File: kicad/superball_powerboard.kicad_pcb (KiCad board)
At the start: 4 copper layers, 100 x 50 mm, 149 parts, among them J1 MICROCLASP_HDRX3, J2 MICROCLASP_HDRX3, J3 MICROCLASP_HDRX2, J4 MICROCLASP_HDRX2, J5 MICROCLASP_HDRX2, J6 MICROCLASP_HDRX2, J7 MICROCLASP_HDRX2, J8 MICROCLASP_HDRX2, J9 MICROCLASP_HDRX2, Q1 MCP73832, Q10 FDS6898AZ, Q11 FDS6898AZ, Q12 LTC1982, Q13 LTC1982, Q14 FDS6898AZ, Q15 FDS6898AZ, Q16 RF803D, Q2 LM3478, Q3 TPS54540, Q4 LT1910, Q5 0S102011MA1QN1, Q6 PSMN013-80YS, Q7 PSMN013-80YS, Q8 LTC1982, Q9 ACS711KLCTR-12AB-T, U1 SI1970DH, U2 CSD16323Q3, U3 SN65HVD232, U4 DSPIC33E128MC506, U5 LDO 3V3 SOT-223

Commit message: started organizing the pcb layout
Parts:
- added ?: P***, 1pin_3mm, F.Cu at (116.6, 24.5)
- added ?: P***, 1pin_3mm, F.Cu at (116.6, 64.8)
- added ?: P***, 1pin_3mm, F.Cu at (23.5, 24.5)
- added ?: P***, 1pin_3mm, F.Cu at (23.5, 64.8)
- added R55: 10K, SM0805, F.Cu at (75.0, 85.0)
- added R56: 10K, SM0805, F.Cu at (70.0, 82.8)
- moved JP11 196.4 mm to (26.0, 54.0)
- moved JP12 133.1 mm to (27.0, 41.0), turned to 90 degrees
- moved JP8 127.0 mm to (85.5, 53.0), turned to 90 degrees
- moved JP6 99.7 mm to (116.5, 40.5), turned to 90 degrees
- moved JP7 96.3 mm to (85.5, 59.0), turned to 90 degrees
- moved C1 74.7 mm to (114.0, 53.5), turned to 90 degrees
- moved JP5 69.1 mm to (61.0, 67.5)
- moved JP4 35.7 mm to (28.5, 31.5), turned to 180 degrees
- moved J9 34.7 mm to (57.0, 68.0), turned to 180 degrees
- moved Q9 23.6 mm to (113.5, 47.5)
- moved J8 20.5 mm to (48.5, 68.0)
- moved JP1 18.5 mm to (34.0, 67.5)
- moved U3 16.6 mm to (48.0, 33.5)
- moved Q5 14.5 mm to (80.5, 68.0)
- moved JP10 7.24 mm to (22.5, 47.5)
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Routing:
- net N-0000041: track 0.00 -> 22.2 mm
- net /CAN_L: track 21.3 -> 1.04 mm
- net /CAN_H: track 15.3 -> 33.6 mm
- net GND: track 0.00 -> 16.2 mm
- net (no net): track 0.00 -> 8.09 mm

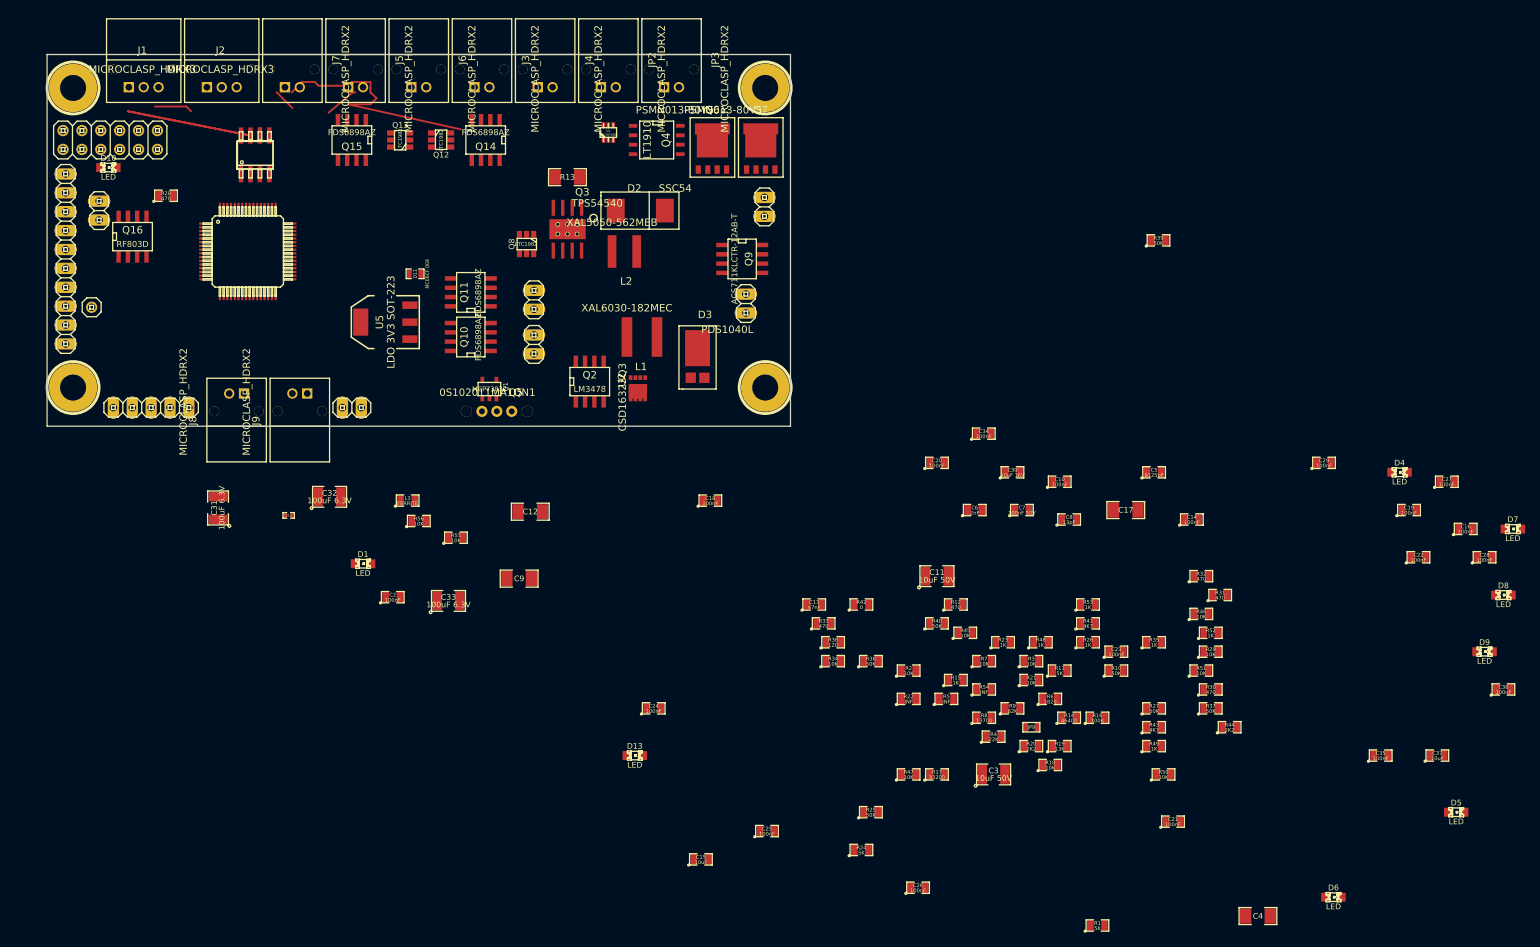
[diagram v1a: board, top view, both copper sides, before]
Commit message: did initial placement of the components on the pcb
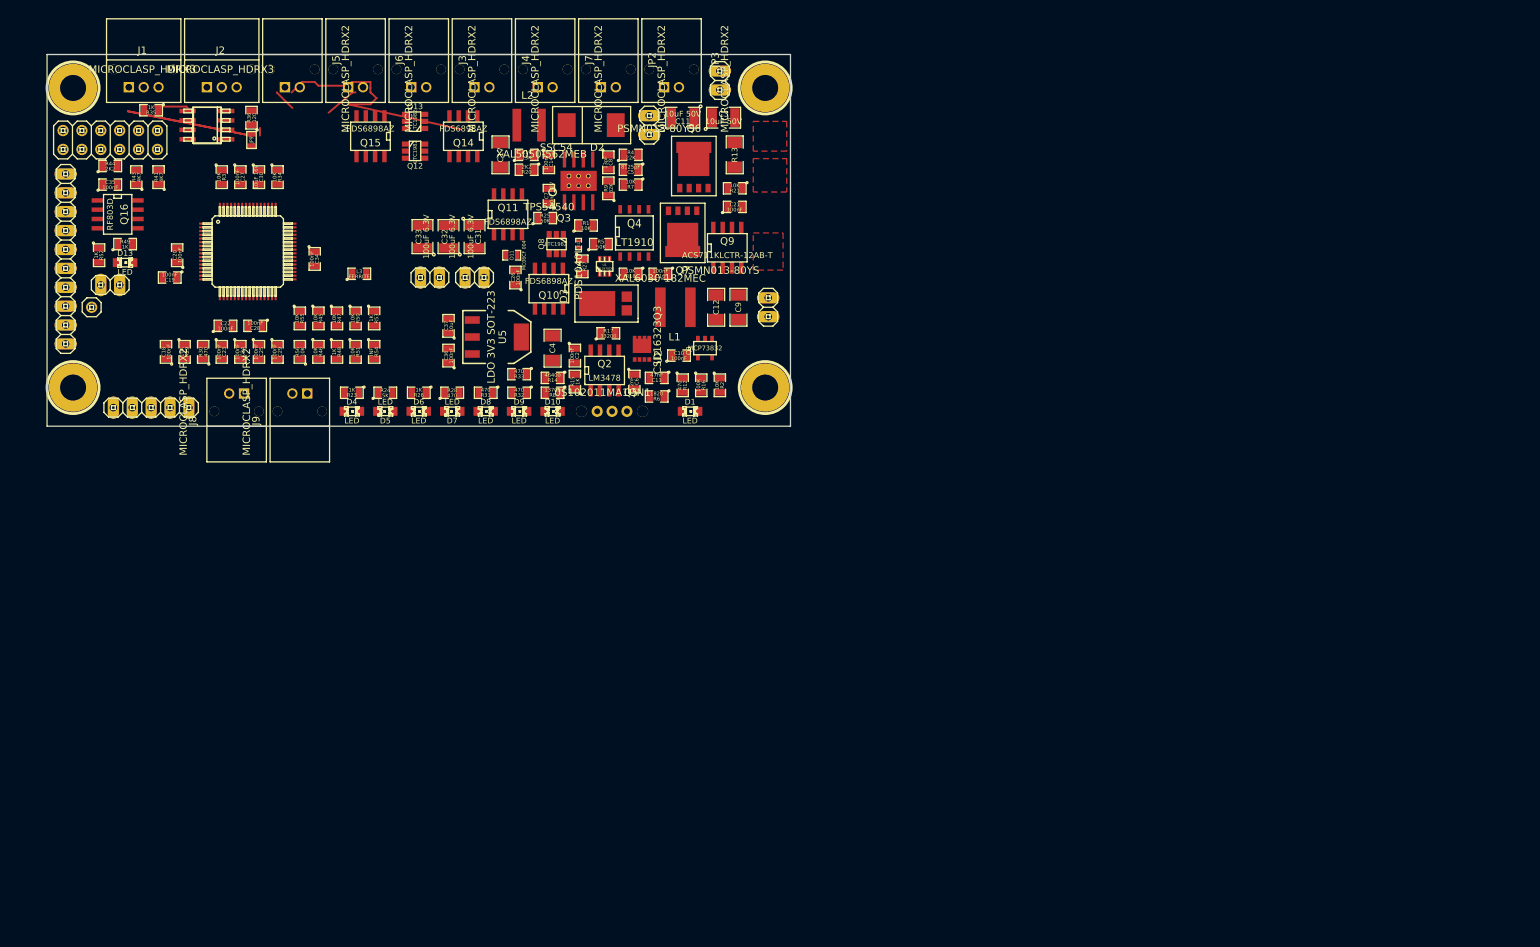
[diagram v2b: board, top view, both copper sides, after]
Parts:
- removed C15: 10uF, SM0805
- removed R10, R37, R38, R39, R40: 50K, SM0805
- removed R11: 5K, SM0805
- removed R22: INF, SM0805
- removed R42: 0, SM0805
- R1: value 5K -> 10K
- R5: value INF -> 50K
- moved C35 187.4 mm to (28.5, 37.5)
- moved C19 169.6 mm to (36.5, 50.0), turned to 180 degrees
- moved R44 168.4 mm to (28.5, 35.0)
- moved C28 168.3 mm to (48.0, 56.5), turned to 180 degrees
- moved C27 167.4 mm to (46.0, 36.5), turned to 270 degrees
- moved C22 163.5 mm to (44.0, 56.5)
- moved R52 157.9 mm to (27.0, 47.0), turned to 270 degrees
- moved R43 155.6 mm to (32.0, 36.5), turned to 90 degrees
- moved R49 154.0 mm to (30.5, 45.5)
- moved D5 153.8 mm to (65.5, 68.0), turned to 180 degrees
- moved R35 152.7 mm to (34.0, 27.5), turned to 180 degrees
- moved C36 148.8 mm to (74.0, 60.5), turned to 90 degrees
- moved C37 145.0 mm to (74.0, 56.5), turned to 90 degrees
- moved R29 143.8 mm to (38.5, 60.0), turned to 270 degrees
- moved D7 143.5 mm to (74.5, 68.0), turned to 180 degrees
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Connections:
- C21 pad 1: 3V3 -> /EN_MOTOR_CURRENT
- Q2 pad 7: N-0000064 (its old number) -> N-0000068
- Q5 pad 1: N-000004 (its old number) -> N-0000060
- Q9 pad 6: N-000009 (its old number) -> /MOTOR_CURRENT_FLT
- Q9 pad 8: 3V3 -> /EN_MOTOR_CURRENT
- R15 pad 1: N-000004 (its old number) -> N-0000060
- R15 pad 2: N-0000064 (its old number) -> N-0000068
- R17 pad 1: N-000004 (its old number) -> N-0000068
- R34 pad 2: N-000009 (its old number) -> /MOTOR_CURRENT_FLT
- R44 pad 2: N-0000059 -> GND
- U4 pad 58: N-0000090 (its old number) -> /MOTOR_CURRENT_FLT
- U4 pad 59: N-00000101 (its old number) -> /EN_MOTOR_CURRENT
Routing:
- net N-0000046: track 0.00 -> 33.6 mm
- net /CAN_H: track 33.6 -> 0.00 mm
- net N-0000031: track 22.2 -> 0.00 mm
- net GND: track 16.2 -> 33.8 mm
- net N-00000110: track 0.00 -> 5.13 mm
- net /CAN_L: track 1.04 -> 0.00 mm
- net (no net): track 8.09 -> 8.63 mm
- added copper zone on F.Cu, net /VBAT_IN
- added copper zone on F.Cu, net /VMOTOR
- added copper zone on F.Cu, net GND

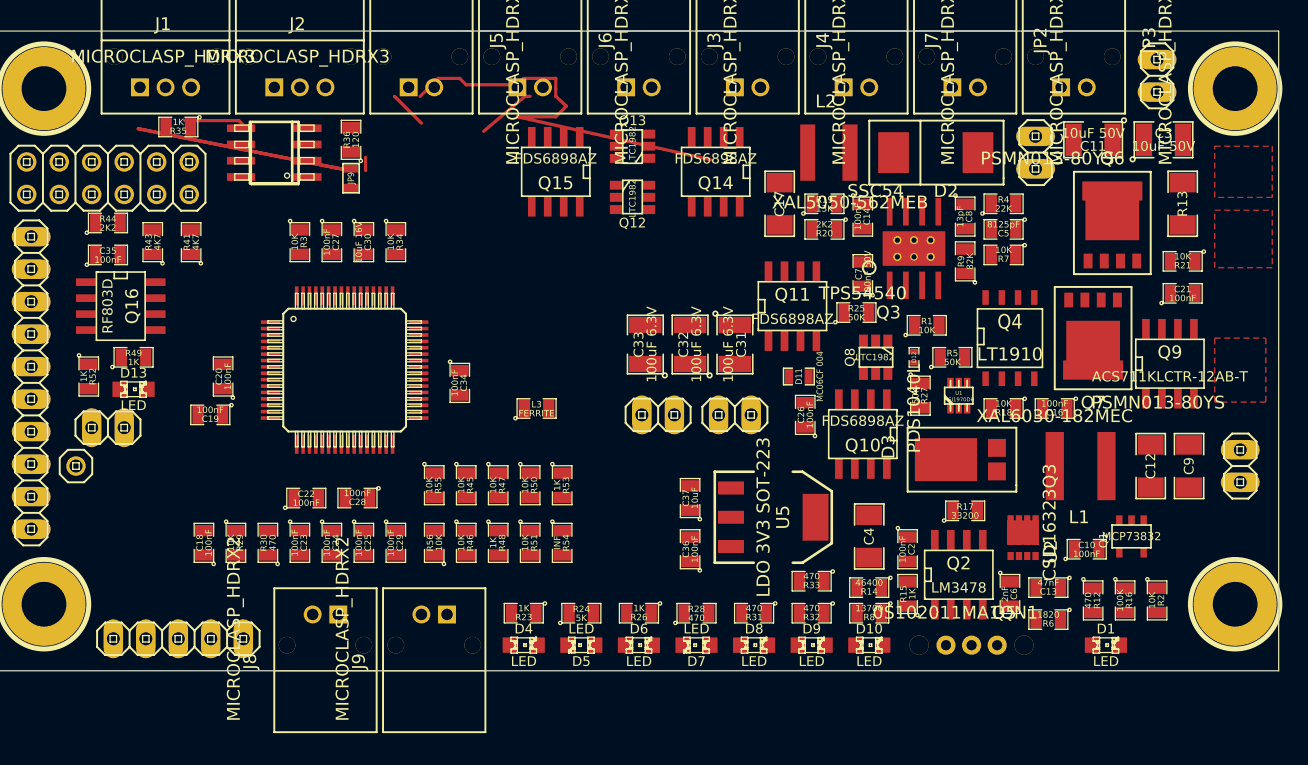
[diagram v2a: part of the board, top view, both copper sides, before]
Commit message: fixed a few bugs in the schematic and started preliminary routing
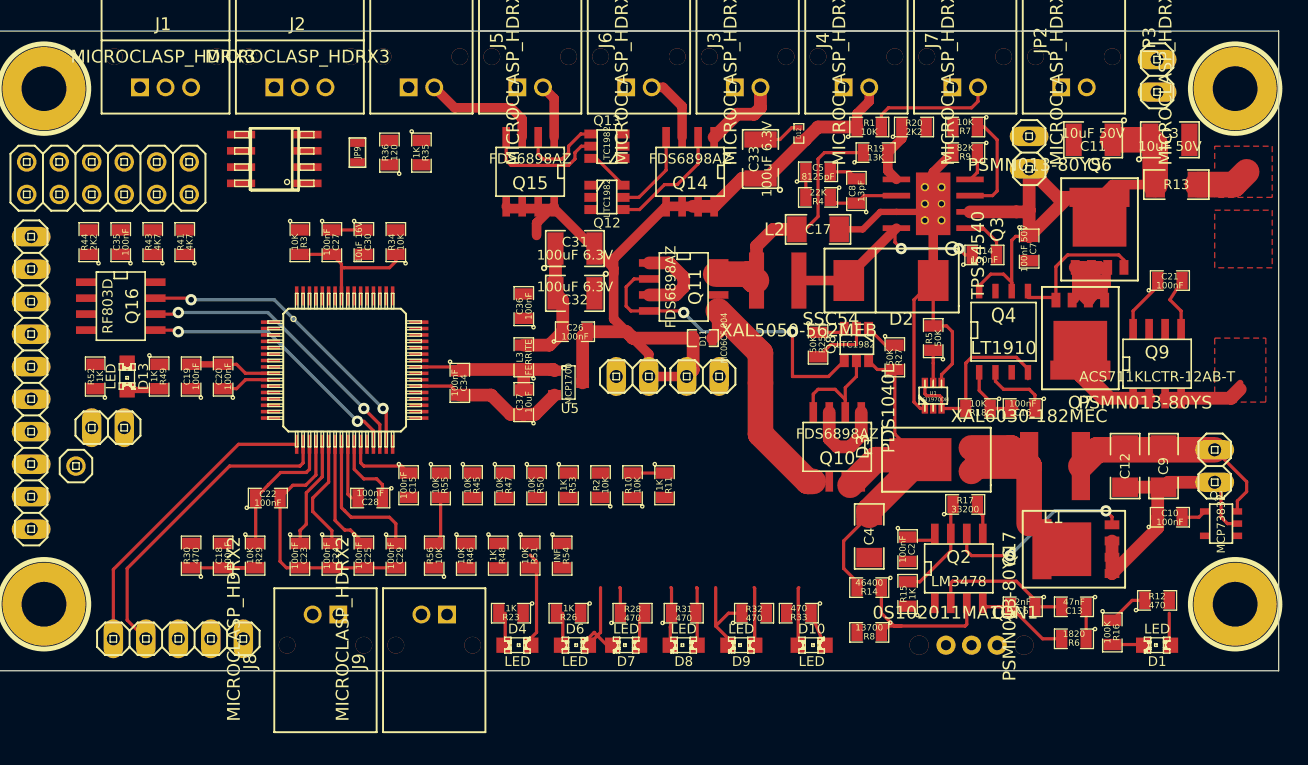
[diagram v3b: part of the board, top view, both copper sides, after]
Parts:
- removed D5: LED, LED-0805
- removed R21: 10K, SM0805
- removed R24: 5K, SM0805
- removed U2: CSD16323Q3, Q3
- added C15: 100nF, SM0805, F.Cu at (52.0, 55.5)
- added Q17: PSMN013-80YS, SOT669, F.Cu at (101.5, 60.5)
- added R10: 10K, SM0805, F.Cu at (69.5, 55.5)
- added R11: 1K, SM0805, F.Cu at (72.0, 55.5)
- U5: value LDO 3V3 SOT-223 -> MCP1700; footprint SOT223 -> SOT23
- moved R2 44.4 mm to (67.0, 55.5), turned to 90 degrees
- moved C36 23.0 mm to (61.0, 41.5)
- moved D12 19.7 mm to (82.5, 28.0), turned to 90 degrees
- moved C26 19.1 mm to (65.0, 43.5), turned to 0 degrees
- moved U5 19.1 mm to (64.5, 47.5)
- moved R35 19.1 mm to (53.0, 29.5), turned to 270 degrees
- moved C33 17.1 mm to (79.5, 30.0)
- moved R1 16.1 mm to (88.0, 27.5)
- moved C5 15.2 mm to (84.0, 31.0), turned to 0 degrees
- moved C37 15.0 mm to (61.0, 49.0)
- moved C31 14.6 mm to (65.0, 37.0), turned to 0 degrees
- moved R4 14.5 mm to (84.0, 33.0), turned to 180 degrees
- moved C7 13.2 mm to (100.5, 37.0), turned to 270 degrees
- moved L2 10.8 mm to (82.5, 39.5)
- moved R20 10.6 mm to (91.5, 27.5), turned to 0 degrees
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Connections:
- ? pad 1: (no net) -> GND
- C8 pad 1: N-0000011 (its old number) -> N-0000014
- Q3 pad 6: (no net) -> N-0000014
- R4 pad 1: N-0000011 (its old number) -> N-0000014
- U4 pad 27: N-0000087 (its old number) -> /VMOTOR_V
- U4 pad 29: /G_BAT_KILL -> /OP3
- U4 pad 31: /OP3 -> /G_BAT_KILL
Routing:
- net GND: track 33.8 -> 162.9 mm
- net /5V5: track 0.00 -> 76.8 mm
- net /VBAT: track 0.00 -> 49.2 mm
- net 3V3: track 0.00 -> 46.7 mm
- net N-0000046: track 33.6 -> 0.00 mm
- net /5V5_VBACKUP: track 0.00 -> 29.5 mm
- net /G_BAT_KILL: track 0.00 -> 26.8 mm, vias 0 -> 2
- net N-0000013: track 0.00 -> 25.4 mm, vias 0 -> 2
- net /PGED: track 0.00 -> 24.7 mm
- net /PGEC: track 0.00 -> 23.8 mm
- net /OP2: track 0.00 -> 22.8 mm, vias 0 -> 2
- net /OP3: track 0.00 -> 21.4 mm, vias 0 -> 2
- net /5V5_VBAT: track 0.00 -> 20.1 mm
- net /VBACKUP: track 0.00 -> 19.4 mm
- net N-0000066: track 0.00 -> 19.0 mm
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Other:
- net class 1mm added: clearance 0.254, trace_width 1, via_dia 0.889, via_drill 0.635
- net class Default: clearance 0.254 -> 0.2
- rule trace_clearance: 0.254 -> 0.2
